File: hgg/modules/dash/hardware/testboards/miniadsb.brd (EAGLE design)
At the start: 39.7 x 47.6 mm, 17 parts, among them IC1 TLC272P, IC2 LM339N, IC3 7414N

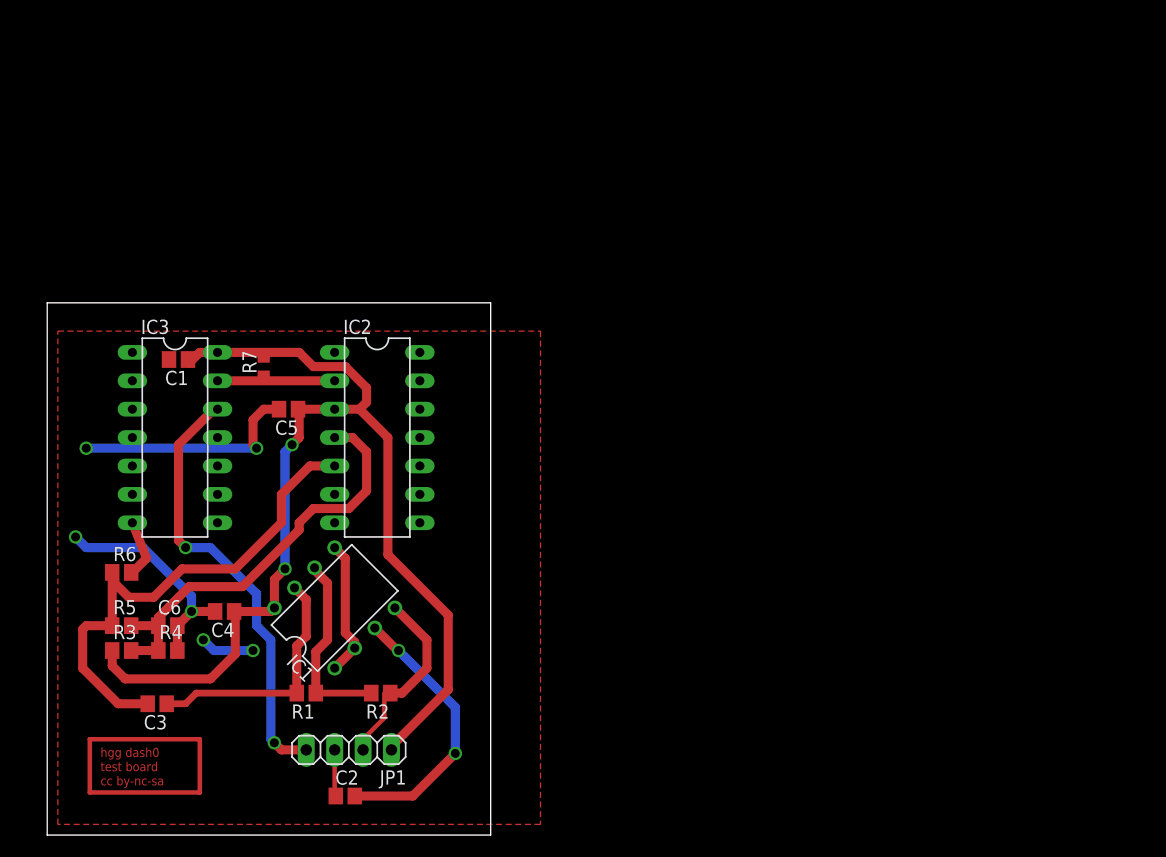
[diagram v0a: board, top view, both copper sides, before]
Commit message: reduced component count, TLC: replaced TRT with SMD variant, layout redone
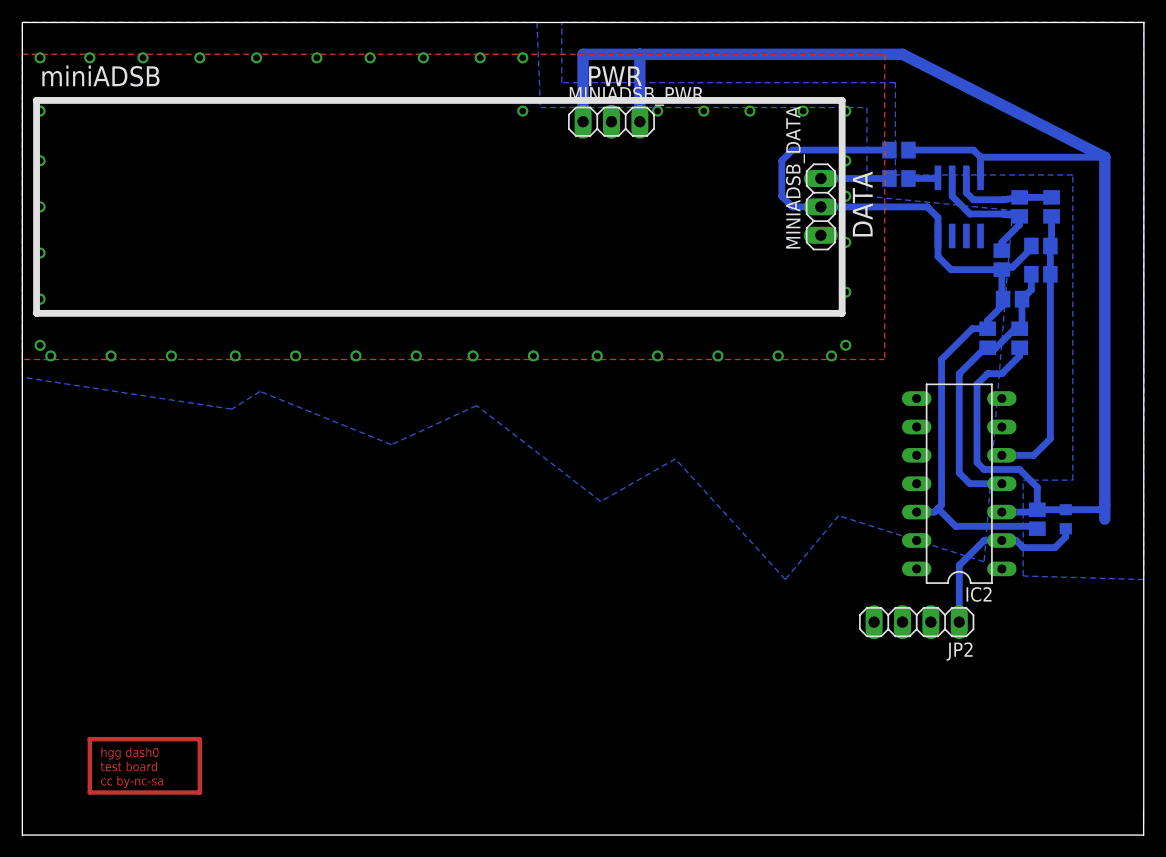
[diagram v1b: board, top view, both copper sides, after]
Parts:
- removed C4: 100n, resistor:C0805
- removed IC3: 7414N, 74xx-us:DIL14
- removed JP1: (no value), pinhead:1X04
- added JP2: (no value), pinhead:1X04
- added MINIADSB_DATA, MINIADSB_PWR: (no value), pinhead:1X03
- IC1: value TLC272P -> TLC272D; device linear:DIL08 -> linear:SO08
- moved C3 91.5 mm to (92.1, 56.2), flipped to the bottom, turned to 270 degrees
- moved R5 88.0 mm to (91.1, 50.2), flipped to the bottom
- moved R6 87.3 mm to (91.1, 52.7), flipped to the bottom
- moved R3 85.0 mm to (89.2, 44.5), flipped to the bottom, turned to 90 degrees
- moved C6 81.0 mm to (88.6, 47.9), flipped to the bottom
- moved R4 78.5 mm to (86.4, 44.5), flipped to the bottom, turned to 90 degrees
- moved C1 78.2 mm to (90.8, 28.3), flipped to the bottom, turned to 270 degrees
- moved R1 77.2 mm to (89.2, 56.2), flipped to the bottom, turned to 90 degrees
- moved C2 74.2 mm to (78.4, 58.7), flipped to the bottom, turned to 180 degrees
- moved R7 73.0 mm to (93.3, 28.3), flipped to the bottom
- moved R2 67.7 mm to (87.6, 51.4), flipped to the bottom, turned to 90 degrees
- moved IC1 66.4 mm to (83.8, 56.2), flipped to the bottom, turned to 0 degrees
- moved C5 59.3 mm to (78.4, 61.3), flipped to the bottom, turned to 0 degrees
- moved IC2 52.2 mm to (83.8, 31.4), turned to 90 degrees
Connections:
- removed net ADSB: IC3.12, JP1.4
- removed net ADSB_IMP: IC1.1, IC1.2, IC1.5
- net /ADSB_TTL: now also JP2.1; no longer IC3.13
- net ADSB_IN: now also MINIADSB_DATA.3; no longer JP1.3
- net GND: now also MINIADSB_DATA.1, MINIADSB_DATA.2, MINIADSB_PWR.2; no longer C4.2, IC3.7, JP1.2
- net N$1: now also IC1.5; no longer IC1.3
- net VCC: now also MINIADSB_PWR.1, MINIADSB_PWR.3; no longer C4.1, IC3.14, JP1.1
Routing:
- net VCC: track 102.3 -> 143.4 mm, vias 2 -> 0
- net ADSB: track 39.5 -> 0.00 mm, vias 2 -> 0
- net N$1: track 24.8 -> 2.67 mm, vias 2 -> 0
- net ADSB_PREAMP: track 45.5 -> 24.9 mm
- net N$2: track 22.2 -> 9.23 mm
- net N$5: track 38.4 -> 25.6 mm
- net ADSB_IMP: track 12.3 -> 0.00 mm
- net GND: track 67.7 -> 77.9 mm, vias 6 -> 41
- net N$3: track 17.4 -> 13.8 mm
- net ADSB_IN: track 4.17 -> 6.14 mm
- net /ADSB_TTL: track 15.0 -> 16.9 mm
- added copper zone on layer 16, net GND
- added copper zone on layer 16, net VCC
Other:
- board size 39.7 x 47.6 mm -> 100.3 x 72.7 mm
- board text added: "DATA"
- board text added: "PWR"
- board text added: "miniADSB"
